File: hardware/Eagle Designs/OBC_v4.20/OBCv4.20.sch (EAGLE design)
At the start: 35 parts, among them J1 MCX-J-P-H-RA-TH1, J10 5037630591, J11 5037630291, J12 5037630491, J13 5037630291, J14 5037630491, J2 5037630491, J3 5037630591, J4 5037630291, J5 5037630291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

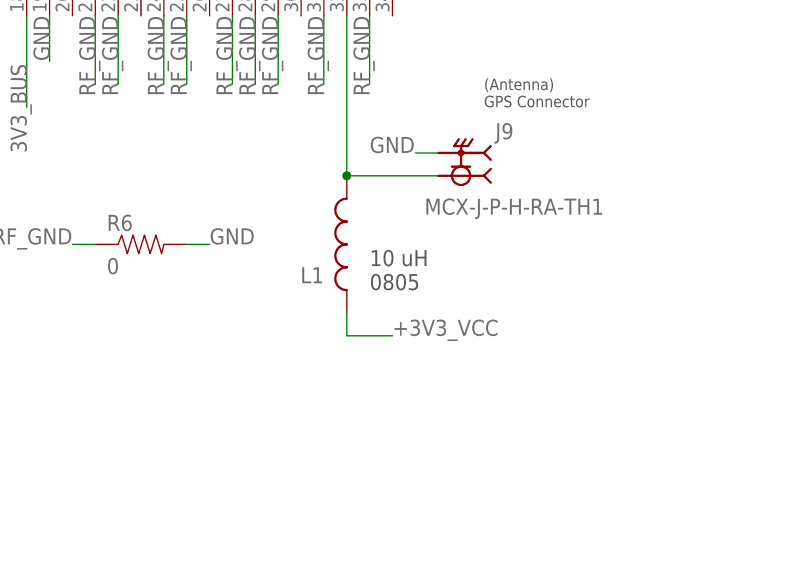
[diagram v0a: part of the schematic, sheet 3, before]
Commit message: revised and finalized OBC v4.20, added OBC v4.20 BOM and Gerber Files
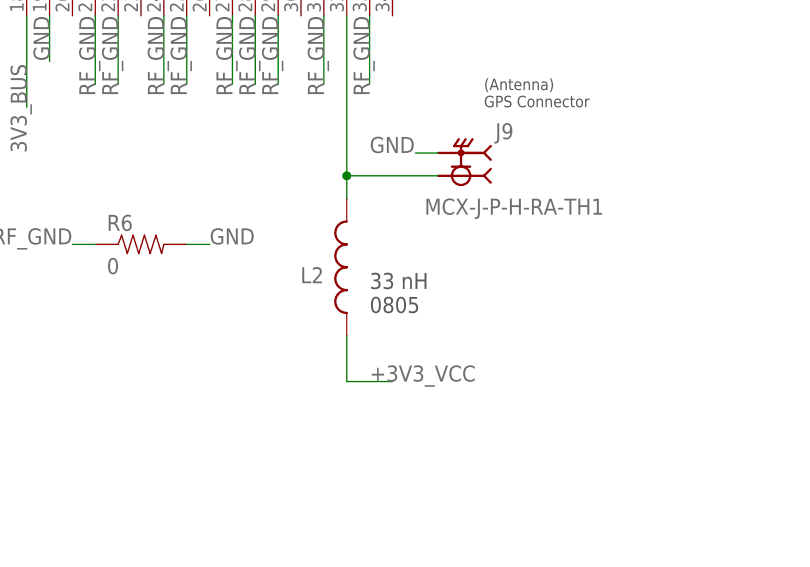
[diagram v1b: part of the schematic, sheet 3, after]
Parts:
- removed L1: L, L:L
- added L2: AIMC-0805-2N2S-T, PDU:AIMC-0805-2N2S-T
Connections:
- net +3V3_VCC: now also L2.1; no longer L1.1
- net N$17: now also L2.2; no longer L1.2
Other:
- note added: "33 nH 0805"
- note removed: "10 uH 0805"
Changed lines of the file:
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@@
 <part name="R4" library="HSFL_Main_Library" deviceset="RESISTOR" device="0805-RES" value="0"/>
 <part name="R5" library="HSFL_Main_Library" deviceset="RESISTOR" device="0805-RES" value="0"/>
-<part name="L1" library="L" deviceset="L" device=""/>
 <part name="R6" library="HSFL_Main_Library" deviceset="RESISTOR" device="0805-RES" value="0"/>
 <part name="U$1" library="OBCv4" deviceset="TEENSY41" device=""/>
@@
 <part name="J9" library="OBCv4" deviceset="MCX-J-P-H-RA-TH1" device=""/>
 <part name="J14" library="OBCv4" deviceset="5037630491" device="" package3d_urn="urn:adsk.eagle:package:30936811/1"/>
+<part name="L2" library="PDU" deviceset="AIMC-0805-2N2S-T" device="" package3d_urn="urn:adsk.eagle:package:30936858/1"/>
 </parts>
 <sheets>
@@
 <text x="-53.34" y="17.78" size="1.27" layer="97">(Antenna)
 GPS Connector</text>
-<text x="-66.04" y="-2.54" size="1.778" layer="97">10 uH
+<text x="-66.04" y="-5.08" size="1.778" layer="97">33 nH
 0805</text>
 </plain>
@@
 <attribute name="VALUE" x="-151.13" y="44.958" size="1.778" layer="96"/>
 </instance>
-<instance part="L1" gate="G$1" x="-68.58" y="2.54" smashed="yes" rot="R90">
-<attribute name="NAME" x="-71.12" y="0" size="1.778" layer="95" rot="R180"/>
-</instance>
 <instance part="R6" gate="G$1" x="-91.44" y="2.54" smashed="yes">
 <attribute name="NAME" x="-95.25" y="4.0386" size="1.778" layer="95"/>
@@
 <attribute name="VALUE" x="-59.944" y="5.842" size="1.778" layer="96"/>
 </instance>
+<instance part="L2" gate="G$1" x="-68.58" y="0" smashed="yes" rot="R90">
+<attribute name="NAME" x="-71.12" y="0" size="1.778" layer="95" rot="R180"/>
+</instance>
 </instances>
 <busses>
@@
 <wire x1="-68.58" y1="27.94" x2="-68.58" y2="10.16" width="0.1524" layer="91"/>
 <wire x1="-58.42" y1="10.16" x2="-68.58" y2="10.16" width="0.1524" layer="91"/>
-<pinref part="L1" gate="G$1" pin="2"/>
+<pinref part="J9" gate="G$1" pin="1"/>
+<pinref part="L2" gate="G$1" pin="2"/>
+<wire x1="-68.58" y1="10.16" x2="-68.58" y2="7.62" width="0.1524" layer="91"/>
 <junction x="-68.58" y="10.16"/>
-<pinref part="J9" gate="G$1" pin="1"/>
 </segment>
 </net>
@@
 </segment>
 <segment>
-<pinref part="L1" gate="G$1" pin="1"/>
-<label x="-63.5" y="-7.62" size="1.778" layer="95"/>
-<wire x1="-68.58" y1="-5.08" x2="-68.58" y2="-7.62" width="0.1524" layer="91"/>
-<wire x1="-68.58" y1="-7.62" x2="-63.5" y2="-7.62" width="0.1524" layer="91"/>
-</segment>
-</net>
+<label x="-66.04" y="-12.7" size="1.778" layer="95"/>
+<wire x1="-68.58" y1="-12.7" x2="-63.5" y2="-12.7" width="0.1524" layer="91"/>
+<pinref part="L2" gate="G$1" pin="1"/>
+<wire x1="-68.58" y1="-12.7" x2="-68.58" y2="-7.62" width="0.1524" layer="91"/>
+</segment>
+</net>
